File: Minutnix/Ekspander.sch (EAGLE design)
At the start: 9 parts, among them SW1 CI-11

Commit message: Wersja 1
Do kubełka 1
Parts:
- renumbered SW1 to ENKODER, U$1 to EKSPANDER, USBASP to EKSP
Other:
- moved on the sheet: R1B, R1C, R1D, R1E, R1F, R1G

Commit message: Archivisation and actualisation
Archivisation of 1 version of boards
New version of boards
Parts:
- removed C3: (no value), rcl:CPOL-EU140CLH-1010
- removed EKSP: (no value), con-harting-ml:ML6
- removed EKSPANDER: PCF8574AT, i2c:PCF8574AT
- removed ENKODER: CI-11, piher:CI-11
- removed S1, S2, S3, S4: (no value), switch:MS243
- added GND, PAD1, PAD10, PAD11, PAD12, PAD13, PAD14, PAD2, PAD3, PAD4, PAD5, PAD6, PAD7, PAD8, PAD9, VCC: WIREPADSMD5-2,5, wirepad:WIREPADSMD5-2,5
- added R0, R2, R3, R4, R5, R6: 220, rcl:R-EU_01005
- added R10, R11, R12, R13, R7, R8, R9: 4.7k, rcl:R-EU_01005
- added S10, S5, S6, S7, S8, S9: MOMENTARY-SWITCH-SPST-LED-PTH-12MM, SparkFun-Switches:MOMENTARY-SWITCH-SPST-LED-PTH-12MM
- added S11: ENCODER-SWITCH, SparkFun-Switches:ENCODER-SWITCH
- R1: value (none) -> 4.7k; device resistor-bourns:2NBS08-7E -> rcl:R-EU_01005
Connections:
- removed net GND: C3.-, EKSP.6, EKSPANDERIC$1.A0, EKSPANDERIC$1.A1, EKSPANDERIC$1.A2, EKSPANDERPWR.GND, ENKODERA.C, ENKODERB.E, S1.S, S2.S, S3.S, S4.S
- new net N$12: PAD14.P, R0.1
- new net N$13: PAD1.P, R11.2, S10.1
- new net N$14: PAD8.P, R13.1, S11.B
- new net N$15: PAD7.P, R12.2, S11.A
- new net N$16: PAD6.P, R1.2, S5.1
- new net N$17: PAD5.P, R7.2, S6.1
- new net N$18: PAD4.P, R8.2, S7.1
- new net N$19: PAD3.P, R9.2, S8.1
- new net N$20: PAD2.P, R10.2, S9.1
- new net N$21: R1.1, R10.1, R11.1, R12.1, R13.2, R7.1, R8.1, R9.1, VCC.P
- new net N$85: GND.P, S10.2, S10.C, S11.C, S5.2, S5.C, S6.2, S6.C, S7.2, S7.C, S8.2, S8.C, S9.2, S9.C
- net N$1: now also R0.2, S5.A; no longer EKSP.5, EKSPANDERIC$1./INT
- net N$10: now also PAD12.P, R3.1; no longer EKSPANDERIC$1.P1, R1F.1, S2.P
- net N$11: now also PAD13.P, R2.1; no longer EKSPANDERIC$1.P0, R1G.1, S1.P
- net N$2: now also R2.2, S6.A; no longer EKSP.1, EKSPANDERIC$1.SDA
- net N$3: now also R3.2, S7.A; no longer EKSP.3, EKSPANDERIC$1.SCL
- net N$4: now also R4.2, S8.A; no longer C3.+, EKSP.2, EKSPANDERPWR.VCC, R1A.2
- net N$5: now also R5.2, S9.A; no longer EKSPANDERIC$1.P7, ENKODERB.D, R1A.1
- net N$6: now also R6.2, S10.A; no longer EKSPANDERIC$1.P6, ENKODERA.B, R1B.1
- net N$7: now also PAD9.P, R6.1; no longer EKSPANDERIC$1.P5, ENKODERA.A, R1C.1
- net N$8: now also PAD10.P, R5.1; no longer EKSPANDERIC$1.P3, R1D.1, S4.P
- net N$9: now also PAD11.P, R4.1; no longer EKSPANDERIC$1.P2, R1E.1, S3.P

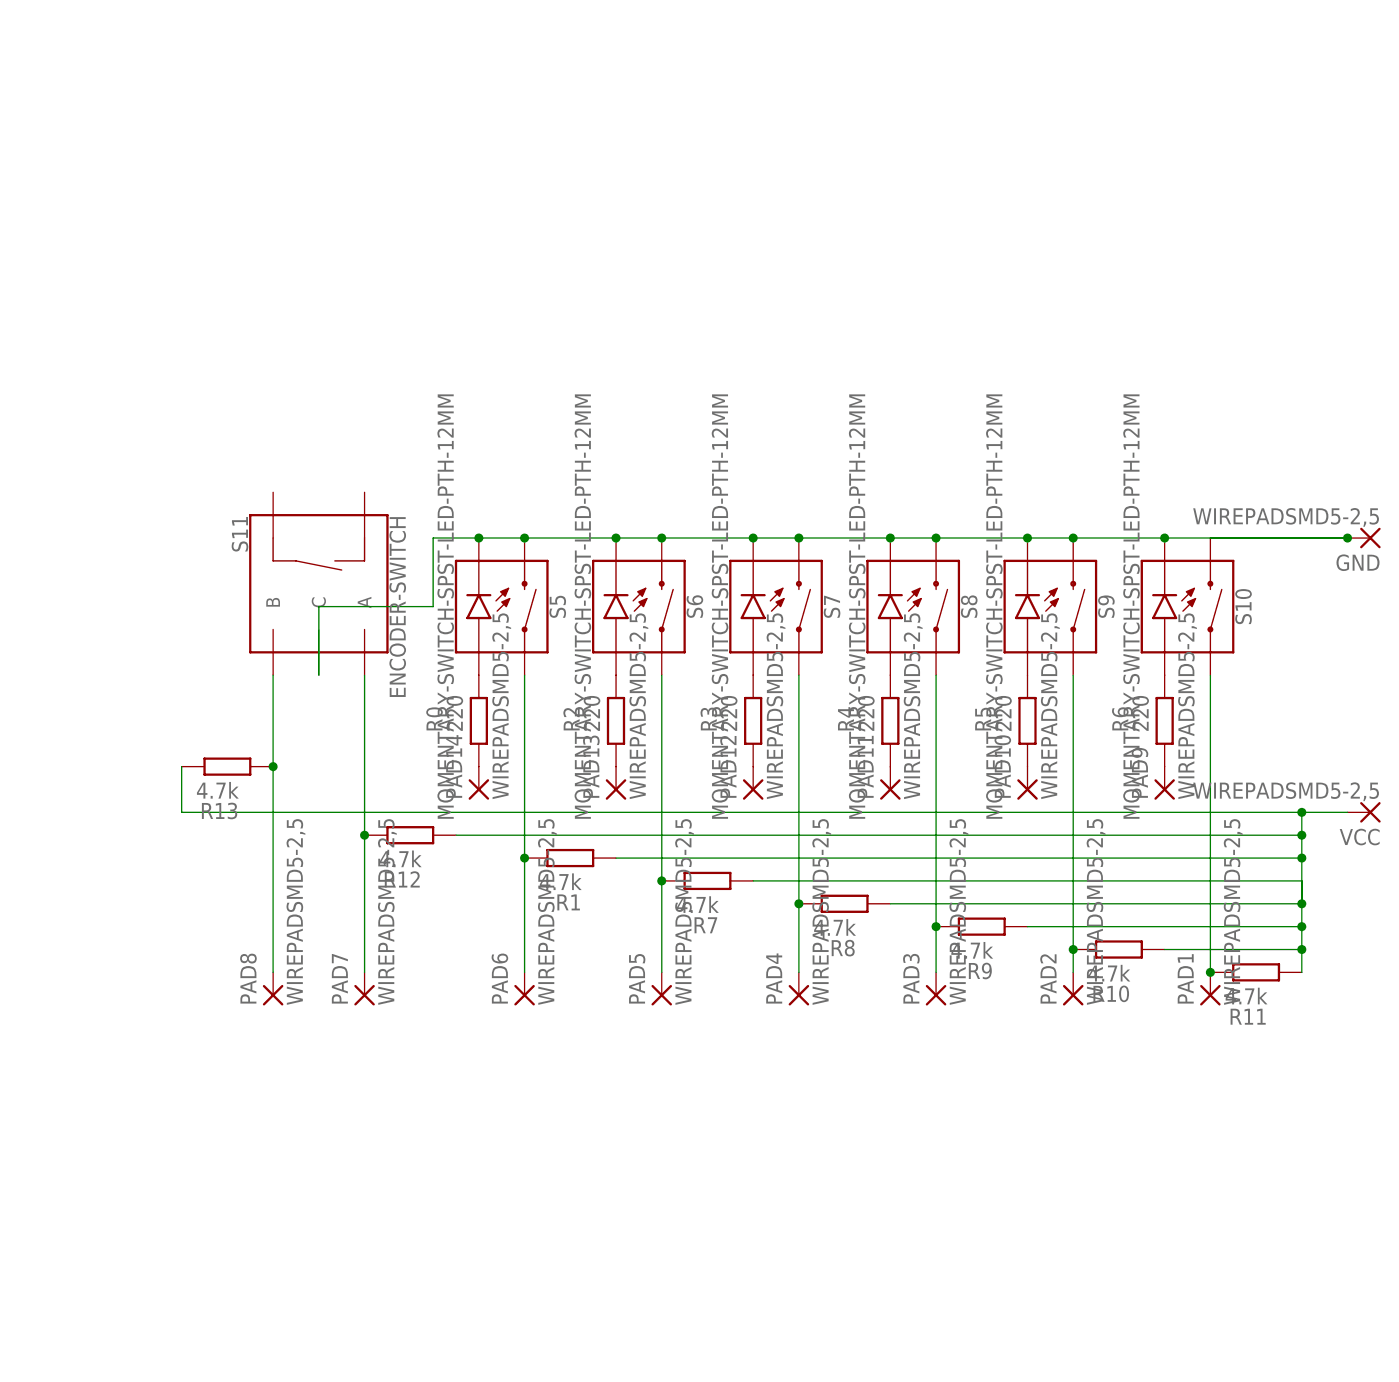
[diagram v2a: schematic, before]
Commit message: Newest Corrected schematic
Splited into diffrent sheets. Improoved readability.
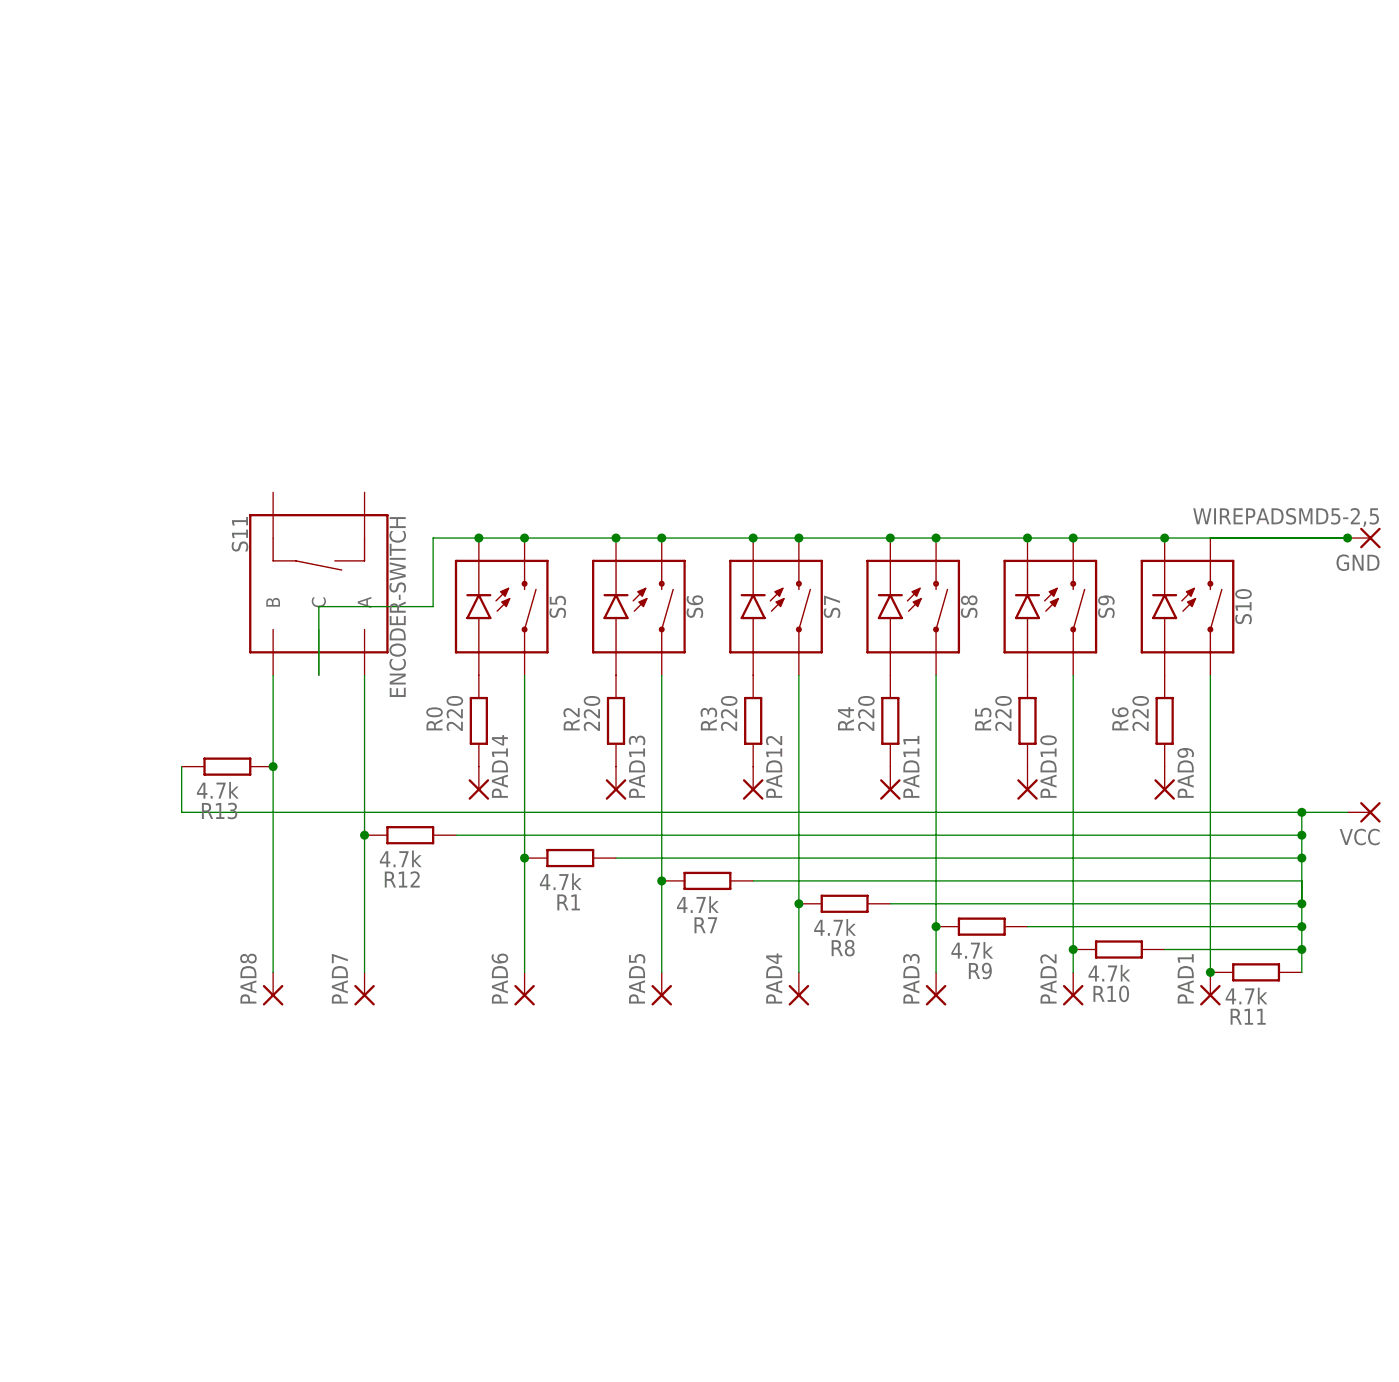
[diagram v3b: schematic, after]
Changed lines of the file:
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@@
 <instance part="S5" gate="G$1" x="35.56" y="144.78" smashed="yes" rot="MR90">
 <attribute name="NAME" x="40.894" y="144.78" size="1.778" layer="95" font="vector" rot="MR90" align="bottom-center"/>
-<attribute name="VALUE" x="30.226" y="144.78" size="1.778" layer="96" font="vector" rot="MR90" align="top-center"/>
 </instance>
 <instance part="S6" gate="G$1" x="50.8" y="144.78" smashed="yes" rot="MR90">
 <attribute name="NAME" x="56.134" y="144.78" size="1.778" layer="95" font="vector" rot="MR90" align="bottom-center"/>
-<attribute name="VALUE" x="45.466" y="144.78" size="1.778" layer="96" font="vector" rot="MR90" align="top-center"/>
 </instance>
 <instance part="S7" gate="G$1" x="66.04" y="144.78" smashed="yes" rot="MR90">
 <attribute name="NAME" x="71.374" y="144.78" size="1.778" layer="95" font="vector" rot="MR90" align="bottom-center"/>
-<attribute name="VALUE" x="60.706" y="144.78" size="1.778" layer="96" font="vector" rot="MR90" align="top-center"/>
 </instance>
 <instance part="S8" gate="G$1" x="81.28" y="144.78" smashed="yes" rot="MR90">
 <attribute name="NAME" x="86.614" y="144.78" size="1.778" layer="95" font="vector" rot="MR90" align="bottom-center"/>
-<attribute name="VALUE" x="75.946" y="144.78" size="1.778" layer="96" font="vector" rot="MR90" align="top-center"/>
 </instance>
 <instance part="S9" gate="G$1" x="96.52" y="144.78" smashed="yes" rot="MR90">
 <attribute name="NAME" x="101.854" y="144.78" size="1.778" layer="95" font="vector" rot="MR90" align="bottom-center"/>
-<attribute name="VALUE" x="91.186" y="144.78" size="1.778" layer="96" font="vector" rot="MR90" align="top-center"/>
 </instance>
 <instance part="S10" gate="G$1" x="111.76" y="144.78" smashed="yes" rot="MR90">
 <attribute name="NAME" x="117.094" y="144.78" size="1.778" layer="95" font="vector" rot="MR90" align="bottom-center"/>
-<attribute name="VALUE" x="106.426" y="144.78" size="1.778" layer="96" font="vector" rot="MR90" align="top-center"/>
 </instance>
 <instance part="S11" gate="G$1" x="15.24" y="147.32" smashed="yes" rot="MR270">
@@
 <instance part="PAD1" gate="G$1" x="114.3" y="101.6" smashed="yes" rot="R90">
 <attribute name="NAME" x="112.4458" y="100.457" size="1.778" layer="95" rot="R90"/>
-<attribute name="VALUE" x="117.602" y="100.457" size="1.778" layer="96" rot="R90"/>
 </instance>
 <instance part="PAD2" gate="G$1" x="99.06" y="101.6" smashed="yes" rot="R90">
 <attribute name="NAME" x="97.2058" y="100.457" size="1.778" layer="95" rot="R90"/>
-<attribute name="VALUE" x="102.362" y="100.457" size="1.778" layer="96" rot="R90"/>
 </instance>
 <instance part="PAD3" gate="G$1" x="83.82" y="101.6" smashed="yes" rot="R90">
 <attribute name="NAME" x="81.9658" y="100.457" size="1.778" layer="95" rot="R90"/>
-<attribute name="VALUE" x="87.122" y="100.457" size="1.778" layer="96" rot="R90"/>
 </instance>
 <instance part="PAD4" gate="G$1" x="68.58" y="101.6" smashed="yes" rot="R90">
 <attribute name="NAME" x="66.7258" y="100.457" size="1.778" layer="95" rot="R90"/>
-<attribute name="VALUE" x="71.882" y="100.457" size="1.778" layer="96" rot="R90"/>
 </instance>
 <instance part="PAD5" gate="G$1" x="53.34" y="101.6" smashed="yes" rot="R90">
 <attribute name="NAME" x="51.4858" y="100.457" size="1.778" layer="95" rot="R90"/>
-<attribute name="VALUE" x="56.642" y="100.457" size="1.778" layer="96" rot="R90"/>
 </instance>
 <instance part="PAD6" gate="G$1" x="38.1" y="101.6" smashed="yes" rot="R90">
 <attribute name="NAME" x="36.2458" y="100.457" size="1.778" layer="95" rot="R90"/>
-<attribute name="VALUE" x="41.402" y="100.457" size="1.778" layer="96" rot="R90"/>
 </instance>
 <instance part="PAD7" gate="G$1" x="20.32" y="101.6" smashed="yes" rot="R90">
 <attribute name="NAME" x="18.4658" y="100.457" size="1.778" layer="95" rot="R90"/>
-<attribute name="VALUE" x="23.622" y="100.457" size="1.778" layer="96" rot="R90"/>
 </instance>
 <instance part="PAD8" gate="G$1" x="10.16" y="101.6" smashed="yes" rot="R90">
 <attribute name="NAME" x="8.3058" y="100.457" size="1.778" layer="95" rot="R90"/>
-<attribute name="VALUE" x="13.462" y="100.457" size="1.778" layer="96" rot="R90"/>
 </instance>
 <instance part="PAD9" gate="G$1" x="109.22" y="124.46" smashed="yes" rot="R90">
-<attribute name="NAME" x="107.3658" y="123.317" size="1.778" layer="95" rot="R90"/>
-<attribute name="VALUE" x="112.522" y="123.317" size="1.778" layer="96" rot="R90"/>
+<attribute name="NAME" x="112.4458" y="123.317" size="1.778" layer="95" rot="R90"/>
 </instance>
 <instance part="PAD10" gate="G$1" x="93.98" y="124.46" smashed="yes" rot="R90">
-<attribute name="NAME" x="92.1258" y="123.317" size="1.778" layer="95" rot="R90"/>
-<attribute name="VALUE" x="97.282" y="123.317" size="1.778" layer="96" rot="R90"/>
+<attribute name="NAME" x="97.2058" y="123.317" size="1.778" layer="95" rot="R90"/>
 </instance>
 <instance part="PAD11" gate="G$1" x="78.74" y="124.46" smashed="yes" rot="R90">
-<attribute name="NAME" x="76.8858" y="123.317" size="1.778" layer="95" rot="R90"/>
-<attribute name="VALUE" x="82.042" y="123.317" size="1.778" layer="96" rot="R90"/>
+<attribute name="NAME" x="81.9658" y="123.317" size="1.778" layer="95" rot="R90"/>
 </instance>
 <instance part="PAD12" gate="G$1" x="63.5" y="124.46" smashed="yes" rot="R90">
-<attribute name="NAME" x="61.6458" y="123.317" size="1.778" layer="95" rot="R90"/>
-<attribute name="VALUE" x="66.802" y="123.317" size="1.778" layer="96" rot="R90"/>
+<attribute name="NAME" x="66.7258" y="123.317" size="1.778" layer="95" rot="R90"/>
 </instance>
 <instance part="PAD13" gate="G$1" x="48.26" y="124.46" smashed="yes" rot="R90">
-<attribute name="NAME" x="46.4058" y="123.317" size="1.778" layer="95" rot="R90"/>
-<attribute name="VALUE" x="51.562" y="123.317" size="1.778" layer="96" rot="R90"/>
+<attribute name="NAME" x="51.4858" y="123.317" size="1.778" layer="95" rot="R90"/>
 </instance>
 <instance part="PAD14" gate="G$1" x="33.02" y="124.46" smashed="yes" rot="R90">
-<attribute name="NAME" x="31.1658" y="123.317" size="1.778" layer="95" rot="R90"/>
-<attribute name="VALUE" x="36.322" y="123.317" size="1.778" layer="96" rot="R90"/>
+<attribute name="NAME" x="36.2458" y="123.317" size="1.778" layer="95" rot="R90"/>
 </instance>
 <instance part="R1" gate="G$1" x="43.18" y="116.84" smashed="yes" rot="R180">
@@
 <instance part="VCC" gate="G$1" x="132.08" y="121.92" smashed="yes" rot="R180">
 <attribute name="NAME" x="133.223" y="120.0658" size="1.778" layer="95" rot="R180"/>
-<attribute name="VALUE" x="133.223" y="125.222" size="1.778" layer="96" rot="R180"/>
 </instance>
 </instances>
